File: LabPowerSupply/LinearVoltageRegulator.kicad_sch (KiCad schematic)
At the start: 14 parts

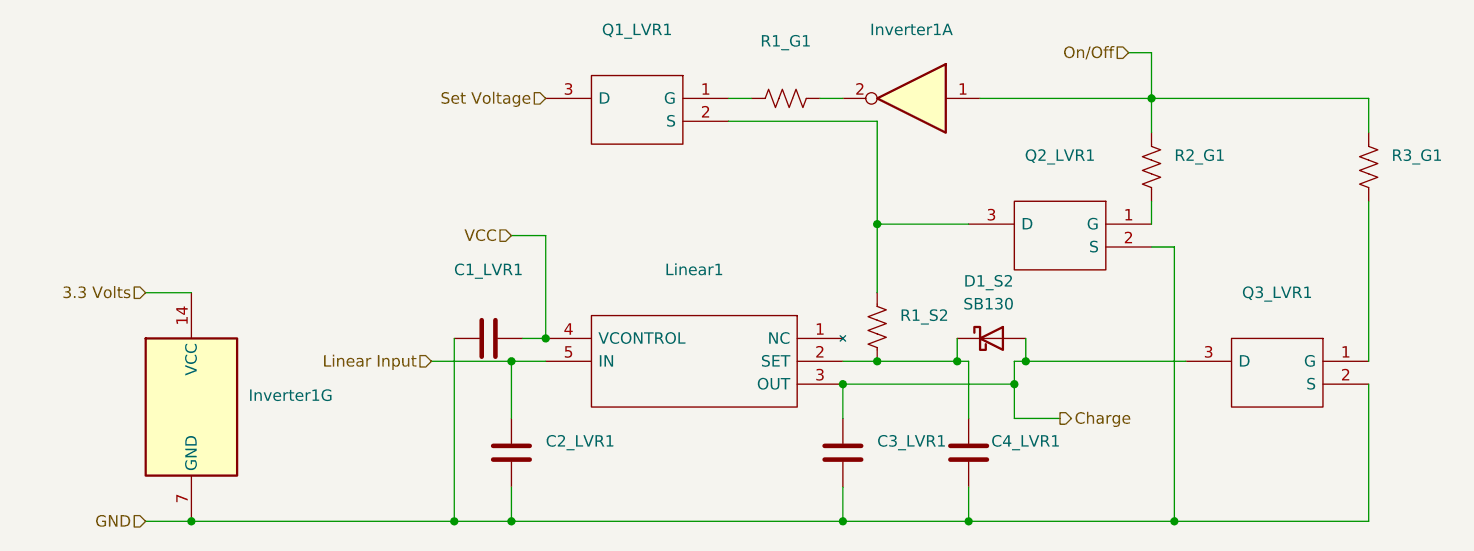
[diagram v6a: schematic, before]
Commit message: Added mcu capacitors, split 5v inductors
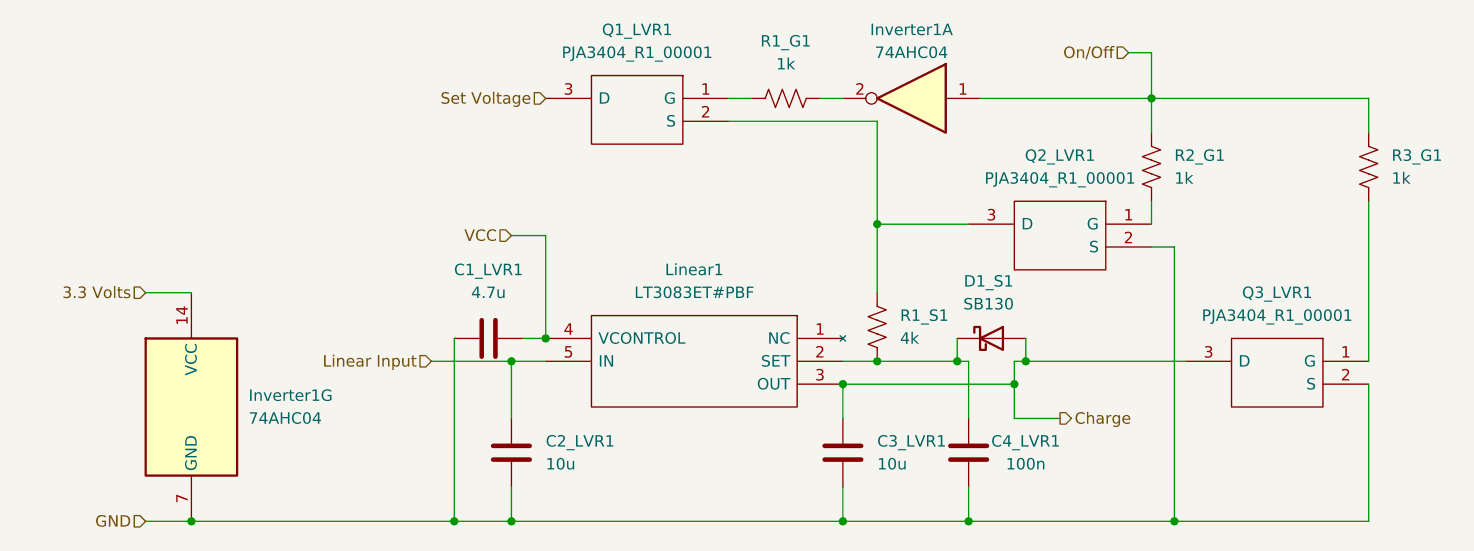
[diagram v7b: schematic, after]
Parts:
- C1_LVR1: value (none) -> 4.7u; footprint (none) -> Capacitor_THT:C_Disc_D5.0mm_W2.5mm_P2.50mm
- C2_LVR1, C3_LVR1: value (none) -> 10u; footprint (none) -> Capacitor_THT:C_Disc_D5.0mm_W2.5mm_P2.50mm
- C4_LVR1: value (none) -> 100n; footprint (none) -> Capacitor_THT:C_Disc_D5.0mm_W2.5mm_P2.50mm
- Inverter1: value (none) -> 74AHC04; footprint (none) -> Package_DIP:DIP-14_W7.62mm
- Linear1: value (none) -> LT3083ET#PBF; footprint (none) -> SamacSys_Parts:TO170P457X1022X2306-5P
- Q1_LVR1, Q2_LVR1, Q3_LVR1: value (none) -> PJA3404_R1_00001; footprint (none) -> SamacSys_Parts:SOT95P240X110-3N
- R1_G1, R2_G1, R3_G1: value (none) -> 1k; footprint (none) -> Resistor_SMD:R_0603_1608Metric
- R1_S1: renamed from R1_S2; value (none) -> 4k
- renumbered D1_S2 to D1_S1
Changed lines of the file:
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@@
     (in_bom yes) (on_board yes) (fields_autoplaced)
     (property "Reference" "Q3_LVR1" (id 0) (at 203.2 90.17 0))
-    (property "Value" "" (id 1) (at 203.2 92.71 0))
-    (property "Footprint" "" (id 2) (at 196.85 95.25 0)
+    (property "Value" "PJA3404_R1_00001" (id 1) (at 203.2 92.71 0))
+    (property "Footprint" "SamacSys_Parts:SOT95P240X110-3N" (id 2) (at 196.85 95.25 0)
       (effects (font (size 1.27 1.27)) (justify left) hide)
     )
@@
       (effects (font (size 1.27 1.27)) (justify left))
     )
-    (property "Value" "" (id 1) (at 88.9 104.1399 0)
-      (effects (font (size 1.27 1.27)) (justify left))
-    )
-    (property "Footprint" "" (id 2) (at 82.55 102.87 0)
+    (property "Value" "74AHC04" (id 1) (at 88.9 104.1399 0)
+      (effects (font (size 1.27 1.27)) (justify left))
+    )
+    (property "Footprint" "Package_DIP:DIP-14_W7.62mm" (id 2) (at 82.55 102.87 0)
       (effects (font (size 1.27 1.27)) hide)
     )
@@
     (in_bom yes) (on_board yes)
     (property "Reference" "Inverter1" (id 0) (at 162.56 60.96 0))
-    (property "Value" "" (id 1) (at 162.56 63.5 0))
-    (property "Footprint" "" (id 2) (at 162.56 68.58 0)
+    (property "Value" "74AHC04" (id 1) (at 162.56 63.5 0))
+    (property "Footprint" "Package_DIP:DIP-14_W7.62mm" (id 2) (at 162.56 68.58 0)
       (effects (font (size 1.27 1.27)) hide)
     )
@@
     (in_bom yes) (on_board yes) (fields_autoplaced)
     (property "Reference" "Q1_LVR1" (id 0) (at 132.08 60.96 0))
-    (property "Value" "" (id 1) (at 132.08 63.5 0))
-    (property "Footprint" "" (id 2) (at 125.73 66.04 0)
+    (property "Value" "PJA3404_R1_00001" (id 1) (at 132.08 63.5 0))
+    (property "Footprint" "SamacSys_Parts:SOT95P240X110-3N" (id 2) (at 125.73 66.04 0)
       (effects (font (size 1.27 1.27)) (justify left) hide)
     )
@@
     (in_bom yes) (on_board yes) (fields_autoplaced)
     (property "Reference" "R1_G1" (id 0) (at 148.59 62.23 90))
-    (property "Value" "" (id 1) (at 148.59 64.77 90))
-    (property "Footprint" "" (id 2) (at 148.844 67.564 90)
+    (property "Value" "1k" (id 1) (at 148.59 64.77 90))
+    (property "Footprint" "Resistor_SMD:R_0603_1608Metric" (id 2) (at 148.844 67.564 90)
       (effects (font (size 1.27 1.27)) hide)
     )
@@
     (in_bom yes) (on_board yes) (fields_autoplaced)
     (property "Reference" "C1_LVR1" (id 0) (at 115.57 87.63 90))
-    (property "Value" "" (id 1) (at 115.57 90.17 90))
-    (property "Footprint" "" (id 2) (at 119.38 94.2848 0)
+    (property "Value" "4.7u" (id 1) (at 115.57 90.17 90))
+    (property "Footprint" "Capacitor_THT:C_Disc_D5.0mm_W2.5mm_P2.50mm" (id 2) (at 119.38 94.2848 0)
       (effects (font (size 1.27 1.27)) hide)
     )
@@
   (symbol (lib_id "Device:R_US") (at 158.75 93.98 180) (unit 1)
     (in_bom yes) (on_board yes) (fields_autoplaced)
-    (property "Reference" "R1_S2" (id 0) (at 161.29 92.7099 0)
-      (effects (font (size 1.27 1.27)) (justify right))
-    )
-    (property "Value" "" (id 1) (at 161.29 95.2499 0)
+    (property "Reference" "R1_S1" (id 0) (at 161.29 92.7099 0)
+      (effects (font (size 1.27 1.27)) (justify right))
+    )
+    (property "Value" "4k" (id 1) (at 161.29 95.2499 0)
       (effects (font (size 1.27 1.27)) (justify right))
     )
@@
     (in_bom yes) (on_board yes) (fields_autoplaced)
     (property "Reference" "Q2_LVR1" (id 0) (at 179.07 74.93 0))
-    (property "Value" "" (id 1) (at 179.07 77.47 0))
-    (property "Footprint" "" (id 2) (at 172.72 80.01 0)
+    (property "Value" "PJA3404_R1_00001" (id 1) (at 179.07 77.47 0))
+    (property "Footprint" "SamacSys_Parts:SOT95P240X110-3N" (id 2) (at 172.72 80.01 0)
       (effects (font (size 1.27 1.27)) (justify left) hide)
     )
@@
       (effects (font (size 1.27 1.27)) (justify right))
     )
-    (property "Value" "" (id 1) (at 215.9 77.4699 0)
-      (effects (font (size 1.27 1.27)) (justify right))
-    )
-    (property "Footprint" "" (id 2) (at 212.344 75.946 90)
+    (property "Value" "1k" (id 1) (at 215.9 77.4699 0)
+      (effects (font (size 1.27 1.27)) (justify right))
+    )
+    (property "Footprint" "Resistor_SMD:R_0603_1608Metric" (id 2) (at 212.344 75.946 90)
       (effects (font (size 1.27 1.27)) hide)
     )
@@
     (in_bom yes) (on_board yes) (fields_autoplaced)
     (property "Reference" "Linear1" (id 0) (at 138.43 87.63 0))
-    (property "Value" "" (id 1) (at 138.43 90.17 0))
-    (property "Footprint" "" (id 2) (at 125.73 92.71 0)
+    (property "Value" "LT3083ET#PBF" (id 1) (at 138.43 90.17 0))
+    (property "Footprint" "SamacSys_Parts:TO170P457X1022X2306-5P" (id 2) (at 125.73 92.71 0)
       (effects (font (size 1.27 1.27)) (justify left) hide)
     )
@@
       (effects (font (size 1.27 1.27)) (justify left))
     )
-    (property "Value" "" (id 1) (at 158.75 109.2199 0)
-      (effects (font (size 1.27 1.27)) (justify left))
-    )
-    (property "Footprint" "" (id 2) (at 155.9052 111.76 0)
+    (property "Value" "10u" (id 1) (at 158.75 109.2199 0)
+      (effects (font (size 1.27 1.27)) (justify left))
+    )
+    (property "Footprint" "Capacitor_THT:C_Disc_D5.0mm_W2.5mm_P2.50mm" (id 2) (at 155.9052 111.76 0)
       (effects (font (size 1.27 1.27)) hide)
     )
@@
   (symbol (lib_id "Diode:SB130") (at 171.45 95.25 0) (unit 1)
     (in_bom yes) (on_board yes) (fields_autoplaced)
-    (property "Reference" "D1_S2" (id 0) (at 171.1325 88.9 0))
+    (property "Reference" "D1_S1" (id 0) (at 171.1325 88.9 0))
     (property "Value" "SB130" (id 1) (at 171.1325 91.44 0))
     (property "Footprint" "Diode_THT:D_DO-41_SOD81_P10.16mm_Horizontal" (id 2) (at 171.45 99.695 0)
@@
       (effects (font (size 1.27 1.27)) (justify right))
     )
-    (property "Value" "" (id 1) (at 191.77 77.4699 0)
-      (effects (font (size 1.27 1.27)) (justify right))
-    )
-    (property "Footprint" "" (id 2) (at 188.214 75.946 90)
+    (property "Value" "1k" (id 1) (at 191.77 77.4699 0)
+      (effects (font (size 1.27 1.27)) (justify right))
+    )
+    (property "Footprint" "Resistor_SMD:R_0603_1608Metric" (id 2) (at 188.214 75.946 90)
       (effects (font (size 1.27 1.27)) hide)
     )
@@
     (in_bom yes) (on_board yes)
     (property "Reference" "C4_LVR1" (id 0) (at 175.26 106.68 0))
-    (property "Value" "" (id 1) (at 175.26 109.22 0))
-    (property "Footprint" "" (id 2) (at 169.8752 111.76 0)
+    (property "Value" "100n" (id 1) (at 175.26 109.22 0))
+    (property "Footprint" "Capacitor_THT:C_Disc_D5.0mm_W2.5mm_P2.50mm" (id 2) (at 169.8752 111.76 0)
       (effects (font (size 1.27 1.27)) hide)
     )
@@
       (effects (font (size 1.27 1.27)) (justify left))
     )
-    (property "Value" "" (id 1) (at 121.92 109.2199 0)
-      (effects (font (size 1.27 1.27)) (justify left))
-    )
-    (property "Footprint" "" (id 2) (at 119.0752 111.76 0)
-      (effects (font (size 1.27 1.27)) hide)
-    )
+    (property "Value" "10u" (id 1) (at 121.92 109.2199 0)
+      (effects (font (size 1.27 1.27)) (justify left))
+    )
+    (property "Footprint" "Capacitor_THT:C_Disc_D5.0mm_W2.5mm_P2.50mm" (id 2) (at 119.0752 111.76 0)
+      (effects (font (size 1.27 1.27)) hide)
+    )
